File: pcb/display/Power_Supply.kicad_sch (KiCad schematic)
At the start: 71 parts, among them Q601 DOZ35N06, Q602 DOZ35N06, U601 SIC438BED-T1-GE3, U602 TPS259474ARPWR, U603 TPS54202DDC, U604 TPS54202DDC, U605 LM74700, U606 LM74700

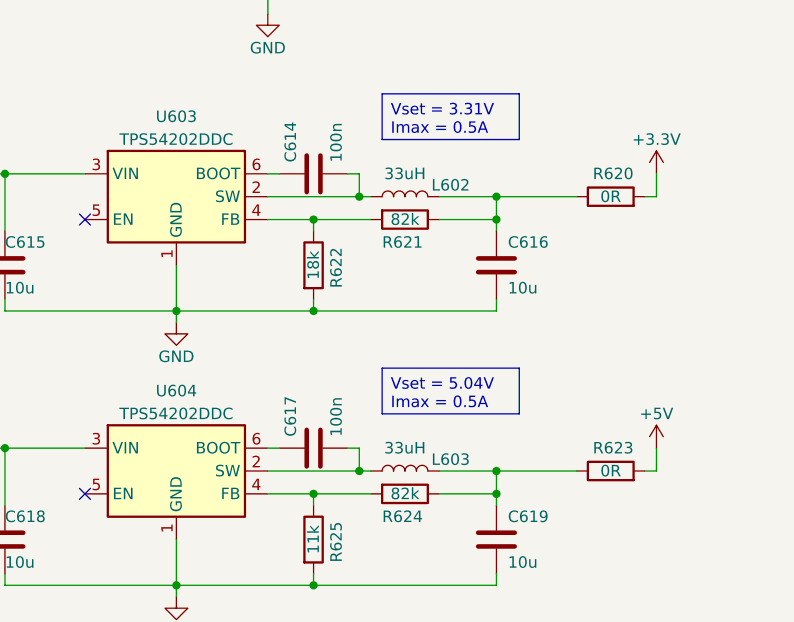
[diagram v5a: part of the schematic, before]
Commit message: OSC Display Hardware Revision 02
There might still be some errors which need to be corrected during ordering.
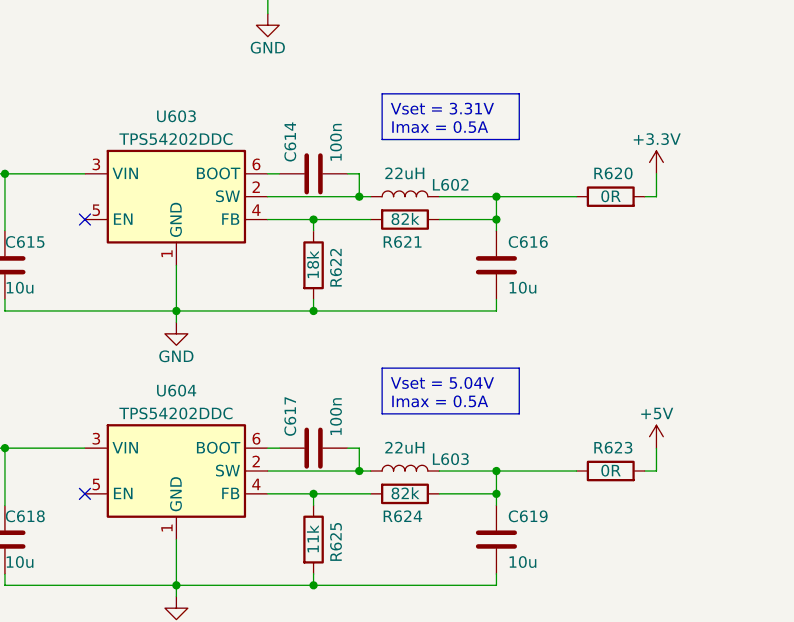
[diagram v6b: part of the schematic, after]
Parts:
- C601, C613, C614, C617, C620, C621: JLC PN C307331 -> (none); LCSC Part # (none) -> C307331
- C602, C603, C606, C615, C618: JLC PN C13585 -> (none); LCSC Part # (none) -> C13585
- C604, C609, C622, C623: JLC PN C15849 -> (none); LCSC Part # (none) -> C15849
- C605: JLC PN C23630 -> (none); LCSC Part # (none) -> C23630
- C607, C608, C612: JLC PN C5373402 -> (none); LCSC Part # (none) -> C5373402
- C610: JLC PN C15195 -> (none); LCSC Part # (none) -> C15195
- C611: JLC PN C1523 -> (none); LCSC Part # (none) -> C1523
- C616, C619: JLC PN C19702 -> (none); LCSC Part # (none) -> C19702
- D601, D602: JLC PN C191023 -> (none); LCSC Part # (none) -> C191023
- D603, D604: JLC PN C20883150 -> (none); LCSC Part # (none) -> C20883150
- D605, D606, D607, D608: JLC PN C2286 -> (none); LCSC Part # (none) -> C2286
- L601: JLC PN C32712978 -> (none); LCSC Part # (none) -> C32712978
- L602, L603: value 33uH -> 22uH; JLC PN C15269 -> (none); LCSC Part # (none) -> C206327
- Q601, Q602: JLC PN C36499167 -> (none); LCSC Part # (none) -> C36499167
- U601: JLC PN C511430 -> (none); LCSC Part # (none) -> C511430
- U602: JLC PN C3662807 -> (none); LCSC Part # (none) -> C3662807
- U603, U604: JLC PN C191884 -> (none); LCSC Part # (none) -> C191884
- U605, U606: JLC PN C2941042 -> (none); LCSC Part # (none) -> C2941042
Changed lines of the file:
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@@
 	(title_block
 		(title "Power Supply")
-		(date "2025-04-11")
-		(rev "01")
+		(date "2026-03-01")
+		(rev "02")
 		(company "Ravenspark")
 		(comment 1 "0-Series")
@@
 			)
 		)
-		(property "JLC PN" "C2941042"
+		(property "LCSC Part #" "C2941042"
 			(at 44.45 102.87 0)
 			(effects
@@
 			)
 		)
-		(property "JLC PN" "C191023"
+		(property "LCSC Part #" "C191023"
 			(at 167.64 74.93 90)
 			(effects
@@
 			)
 		)
-		(property "JLC PN" "C23630"
+		(property "LCSC Part #" "C23630"
 			(at 212.09 53.34 0)
 			(effects
@@
 			)
 		)
-		(property "JLC PN" "C307331"
-			(at 252.73 25.4 0)
+		(property "LCSC Part #" "C307331"
+			(at 252.73 25.4 90)
 			(effects
 				(font
@@
 			)
 		)
-		(property "JLC PN" "C15849"
+		(property "LCSC Part #" "C15849"
 			(at 24.13 114.3 0)
 			(effects
@@
 			)
 		)
-		(property "Value" "33uH"
+		(property "Value" "22uH"
 			(at 243.84 81.28 90)
 			(effects
@@
 			)
 		)
-		(property "JLC PN" "C15269"
-			(at 243.84 83.82 0)
+		(property "LCSC Part #" "C206327"
+			(at 243.84 83.82 90)
 			(effects
 				(font
@@
 			)
 		)
-		(property "JLC PN" "C13585"
+		(property "LCSC Part #" "C13585"
 			(at 182.88 52.07 0)
 			(effects
@@
 			)
 		)
-		(property "Value" "33uH"
+		(property "Value" "22uH"
 			(at 243.84 111.76 90)
 			(effects
@@
 			)
 		)
-		(property "JLC PN" "C15269"
-			(at 243.84 114.3 0)
+		(property "LCSC Part #" "C206327"
+			(at 243.84 114.3 90)
 			(effects
 				(font
@@
 			)
 		)
-		(property "JLC PN" "C2941042"
+		(property "LCSC Part #" "C2941042"
 			(at 45.72 45.72 0)
 			(effects
@@
 			)
 		)
-		(property "JLC PN" "C36499167"
+		(property "LCSC Part #" "C36499167"
 			(at 45.72 27.94 0)
 			(effects
@@
 			)
 		)
-		(property "JLC PN" "C191023"
+		(property "LCSC Part #" "C191023"
 			(at 161.29 81.28 90)
 			(effects
@@
 			)
 		)
-		(property "JLC PN" "C13585"
+		(property "LCSC Part #" "C13585"
 			(at 261.62 53.34 0)
 			(effects
@@
 			)
 		)
-		(property "JLC PN" "C2286"
-			(at 127 173.99 0)
+		(property "LCSC Part #" "C2286"
+			(at 127 173.99 90)
 			(effects
 				(font
@@
 			)
 		)
-		(property "JLC PN" "C1523"
+		(property "LCSC Part #" "C1523"
 			(at 111.76 55.88 0)
 			(effects
@@
 			)
 		)
-		(property "JLC PN" "C3662807"
+		(property "LCSC Part #" "C3662807"
 			(at 97.79 25.4 0)
 			(effects
@@
 			)
 		)
-		(property "JLC PN" "C19702"
+		(property "LCSC Part #" "C19702"
 			(at 254 121.92 0)
 			(effects
@@
 			)
 		)
-		(property "JLC PN" "C2286"
-			(at 144.78 173.99 0)
+		(property "LCSC Part #" "C2286"
+			(at 144.78 173.99 90)
 			(effects
 				(font
@@
 			)
 		)
-		(property "JLC PN" "C307331"
+		(property "LCSC Part #" "C307331"
 			(at 233.68 111.76 0)
 			(effects
@@
 			)
 		)
-		(property "JLC PN" "C191884"
+		(property "LCSC Part #" "C191884"
 			(at 218.44 114.3 0)
 			(effects
@@
 			)
 		)
-		(property "JLC PN" "C191884"
+		(property "LCSC Part #" "C191884"
 			(at 218.44 83.82 0)
 			(effects
@@
 			)
 		)
-		(property "JLC PN" "C307331"
+		(property "LCSC Part #" "C307331"
 			(at 30.48 41.91 0)
 			(effects
@@
 			)
 		)
-		(property "JLC PN" "C13585"
+		(property "LCSC Part #" "C13585"
 			(at 199.39 121.92 0)
 			(effects
@@
 			)
 		)
-		(property "JLC PN" "C307331"
+		(property "LCSC Part #" "C307331"
 			(at 149.86 55.88 0)
 			(effects
@@
 			)
 		)
-		(property "JLC PN" "C15849"
+		(property "LCSC Part #" "C15849"
 			(at 205.74 53.34 0)
 			(effects
@@
 			)
 		)
-		(property "JLC PN" "C2286"
-			(at 135.89 173.99 0)
+		(property "LCSC Part #" "C2286"
+			(at 135.89 173.99 90)
 			(effects
 				(font
@@
 			)
 		)
-		(property "JLC PN" "C19702"
+		(property "LCSC Part #" "C19702"
 			(at 254 91.44 0)
 			(effects
@@
 			)
 		)
-		(property "JLC PN" "C307331"
+		(property "LCSC Part #" "C307331"
 			(at 29.21 99.06 0)
 			(effects
@@
 			)
 		)
-		(property "JLC PN" "C5373402"
+		(property "LCSC Part #" "C5373402"
 			(at 271.78 53.34 0)
 			(effects
@@
 			)
 		)
-		(property "JLC PN" "C511430"
+		(property "LCSC Part #" "C511430"
 			(at 229.87 22.86 0)
 			(effects
@@
 			)
 		)
-		(property "JLC PN" "C36499167"
+		(property "LCSC Part #" "C36499167"
 			(at 44.45 85.09 0)
 			(effects
@@
 			)
 		)
-		(property "JLC PN" "C13585"
+		(property "LCSC Part #" "C13585"
 			(at 199.39 91.44 0)
 			(effects
@@
 			)
 		)
-		(property "JLC PN" "C20883150"
+		(property "LCSC Part #" "C20883150"
 			(at 17.78 114.3 0)
 			(effects
@@
 			)
 		)
-		(property "JLC PN" "C307331"
+		(property "LCSC Part #" "C307331"
 			(at 233.68 81.28 0)
 			(effects
@@
 			)
 		)
-		(property "JLC PN" "C20883150"
+		(property "LCSC Part #" "C20883150"
 			(at 19.05 57.15 0)
 			(effects
@@
 			)
 		)
-		(property "JLC PN" "C5373402"
+		(property "LCSC Part #" "C5373402"
 			(at 279.4 53.34 0)
 			(effects
@@
 			)
 		)
-		(property "JLC PN" "C2286"
-			(at 153.67 173.99 0)
+		(property "LCSC Part #" "C2286"
+			(at 153.67 173.99 90)
 			(effects
 				(font
@@
 			)
 		)
-		(property "JLC PN" "C5373402"
+		(property "LCSC Part #" "C5373402"
 			(at 134.62 55.88 0)
 			(effects
@@
 			)
 		)
-		(property "JLC PN" "C32712978"
-			(at 252.73 35.56 0)
+		(property "LCSC Part #" "C32712978"
+			(at 252.73 35.56 90)
 			(effects
 				(font
@@
 			)
 		)
-		(property "JLC PN" "C15849"
+		(property "LCSC Part #" "C15849"
 			(at 68.58 55.88 0)
 			(effects
@@
 			)
 		)
-		(property "JLC PN" "C15195"
+		(property "LCSC Part #" "C15195"
 			(at 83.82 55.88 0)
 			(effects
@@
 			)
 		)
-		(property "JLC PN" "C13585"
+		(property "LCSC Part #" "C13585"
 			(at 176.53 52.07 0)
 			(effects
@@
 			)
 		)
-		(property "JLC PN" "C15849"
+		(property "LCSC Part #" "C15849"
 			(at 25.4 57.15 0)
 			(effects

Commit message: Adjusted footprint of mosfets for 0.15mm solder mask spacing
New Gerber files
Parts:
- Q601, Q602: footprint Package_SON:VSON-8_3.3x3.3mm_P0.65mm_NexFET -> RVNSPRK_Packages:VSON-8_3.3x3.3mm_P0.65mm_Custom
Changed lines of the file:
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@@
 			)
 		)
-		(property "Footprint" "Package_SON:VSON-8_3.3x3.3mm_P0.65mm_NexFET"
+		(property "Footprint" "RVNSPRK_Packages:VSON-8_3.3x3.3mm_P0.65mm_Custom"
 			(at 48.26 22.86 0)
 			(effects
@@
 			)
 		)
-		(property "Footprint" "Package_SON:VSON-8_3.3x3.3mm_P0.65mm_NexFET"
+		(property "Footprint" "RVNSPRK_Packages:VSON-8_3.3x3.3mm_P0.65mm_Custom"
 			(at 46.99 80.01 0)
 			(effects

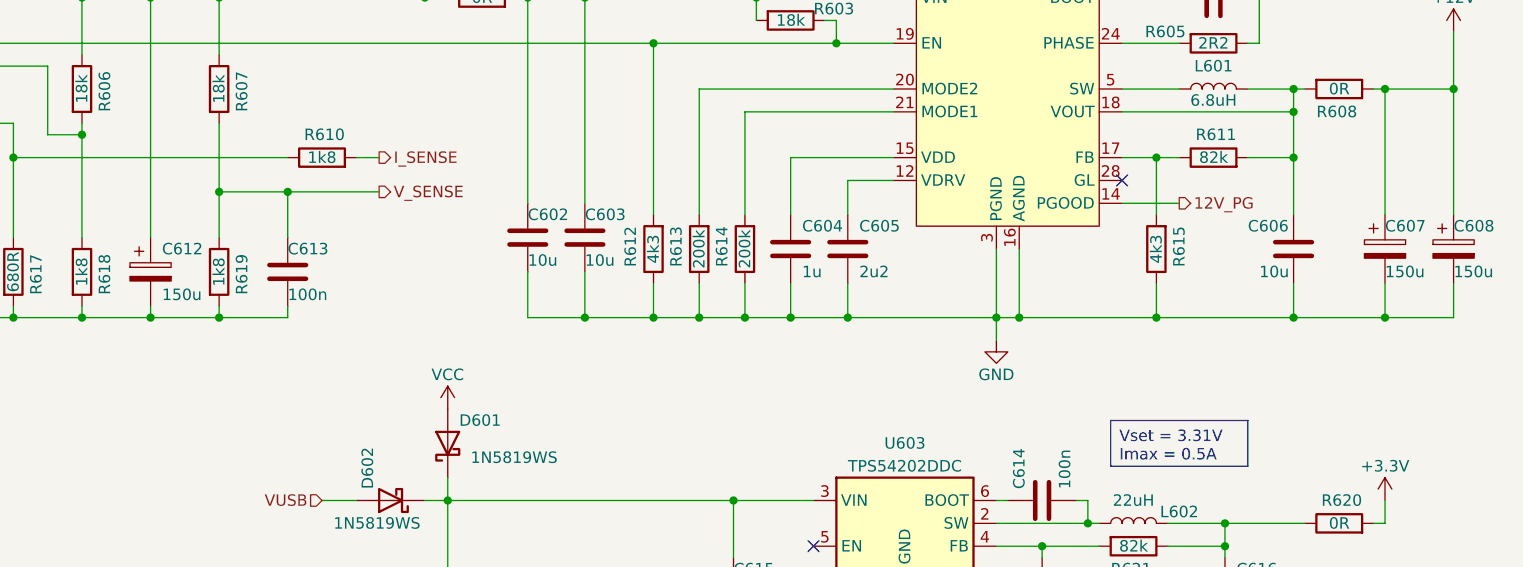
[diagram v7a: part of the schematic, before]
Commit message: Changed some Part# for production based on feedback an availability
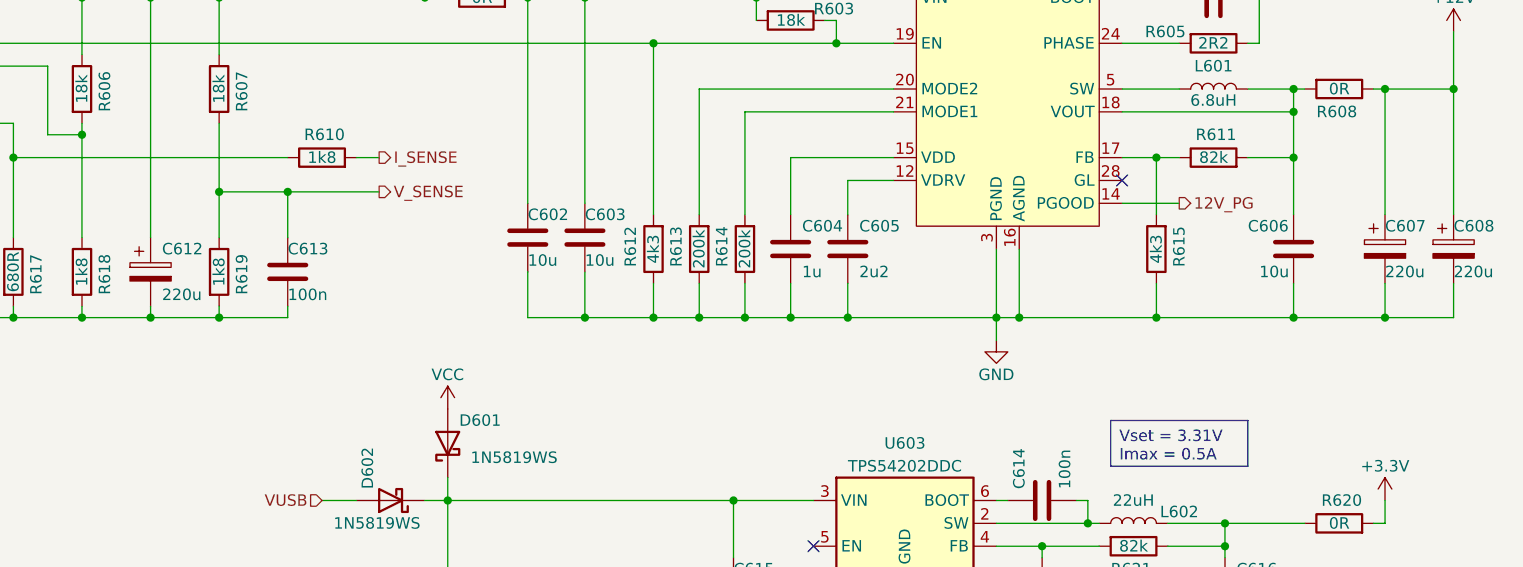
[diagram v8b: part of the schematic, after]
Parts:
- C607, C608, C612: value 150u -> 220u; LCSC Part # C5373402 -> C5246542
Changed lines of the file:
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@@
 			)
 		)
-		(property "Value" "150u"
+		(property "Value" "220u"
 			(at 271.78 55.88 0)
 			(effects
@@
 			)
 		)
-		(property "LCSC Part #" "C5373402"
+		(property "LCSC Part #" "C5246542"
 			(at 271.78 53.34 0)
 			(effects
@@
 			)
 		)
-		(property "Value" "150u"
+		(property "Value" "220u"
 			(at 279.4 55.88 0)
 			(effects
@@
 			)
 		)
-		(property "LCSC Part #" "C5373402"
+		(property "LCSC Part #" "C5246542"
 			(at 279.4 53.34 0)
 			(effects
@@
 			)
 		)
-		(property "Value" "150u"
+		(property "Value" "220u"
 			(at 135.89 58.42 0)
 			(effects
@@
 			)
 		)
-		(property "LCSC Part #" "C5373402"
+		(property "LCSC Part #" "C5246542"
 			(at 134.62 55.88 0)
 			(effects
